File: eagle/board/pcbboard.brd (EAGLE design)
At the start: 70.5 x 43.2 mm, 39 parts, among them U2 ATMEGA328P-PU, Y2 16MHz

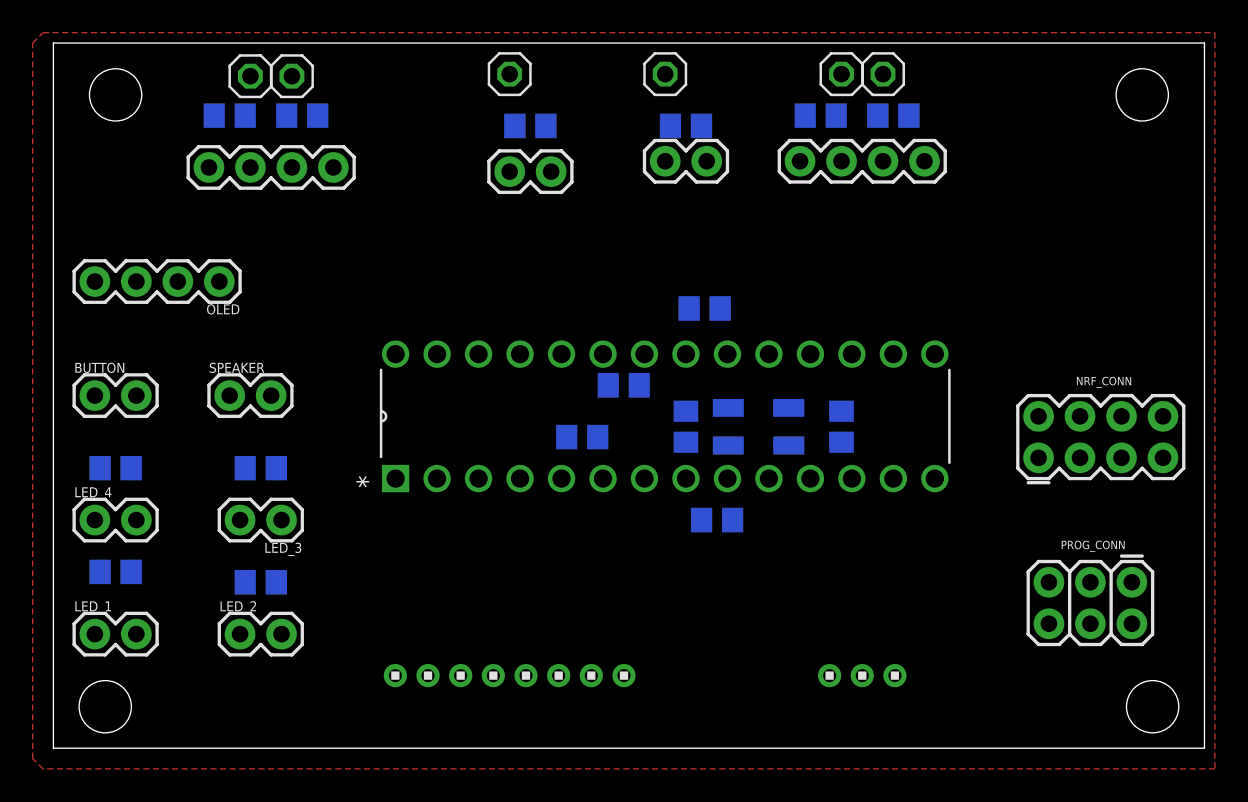
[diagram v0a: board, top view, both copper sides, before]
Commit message: Re organized board
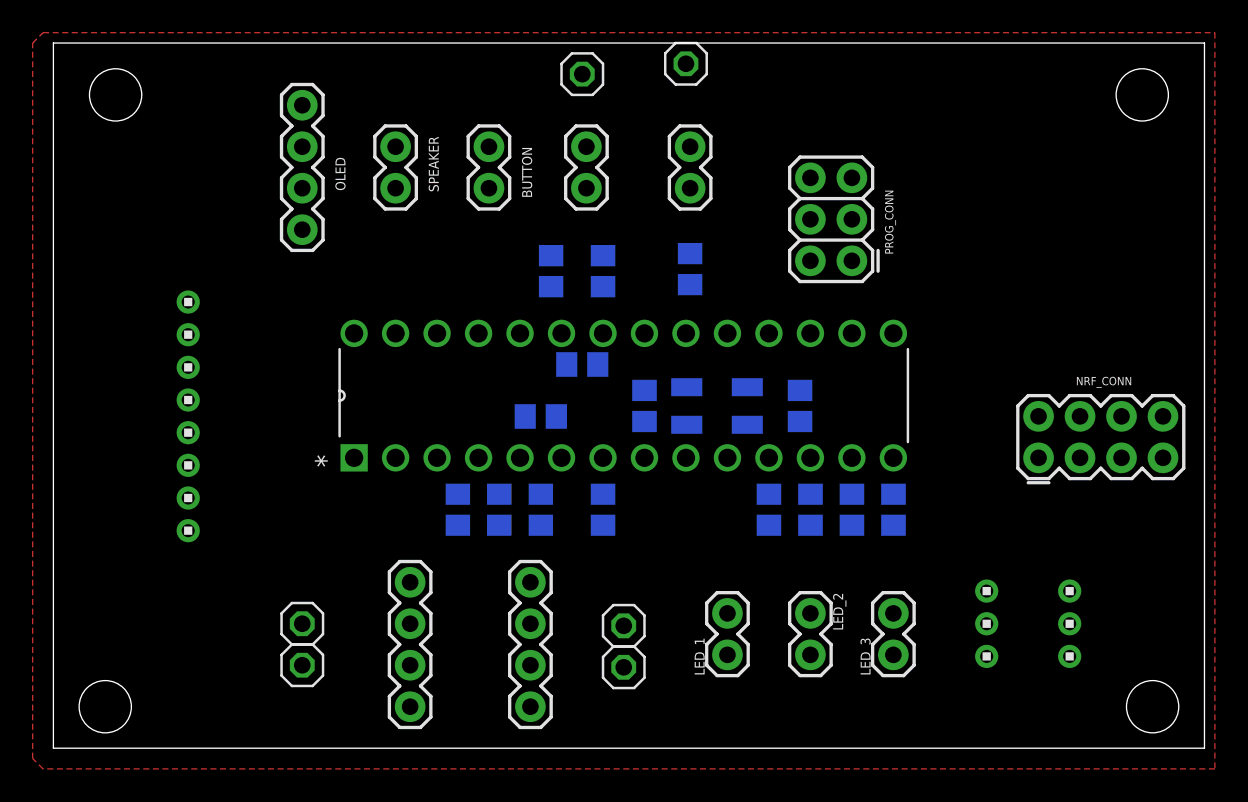
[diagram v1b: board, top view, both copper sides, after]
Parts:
- removed LED_4: (no value), SparkFun-Connectors:1X02
- removed R2: 470, rcl:R0805
- added U$1: 1X3, headers(2mm):1X3
- moved NO_NAME1 49.0 mm to (-5.08, 2.54)
- moved NO_NAME2 49.0 mm to (-5.08, 5.08)
- moved NO_NAME3 42.8 mm to (14.6, 2.41)
- moved R5 41.4 mm to (28.6, 12.1), turned to 90 degrees
- moved HALL_CONN1 41.1 mm to (1.52, 0.00), turned to 90 degrees
- moved R11 40.2 mm to (23.5, 12.1), turned to 270 degrees
- moved NO_NAME4 39.3 mm to (14.6, 4.95)
- moved R9 38.8 mm to (31.1, 12.1), turned to 270 degrees
- moved LED_1 38.8 mm to (21.0, 3.17), turned to 90 degrees
- moved HALL_CONN3 38.4 mm to (8.89, 0.00), turned to 90 degrees
- moved LED_3 38.4 mm to (31.1, 3.17), turned to 90 degrees
- moved LED_2 34.9 mm to (26.0, 5.71), turned to 270 degrees
- moved R10 33.9 mm to (26.0, 12.1), turned to 270 degrees
- moved R4 32.8 mm to (4.45, 12.1), turned to 90 degrees
- moved R3 32.4 mm to (9.53, 12.1), turned to 90 degrees
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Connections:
- removed net N$2: LED_4.2, R2.2
- net +5V: now also U$1.2
- net A2: now also BUTTON.2
- net A3: now also SPEAKER.2
- net D5: now also R11.1
- net D6: now also R10.1, U$1.3; no longer HALL_CONN3.3, NO_NAME4.1, R5.2
- net D7: now also HALL_CONN3.3, NO_NAME4.1, R5.2
- net D8: now also R9.1
- net GND: now also BUTTON.1, SPEAKER.1, U$1.1; no longer LED_4.1
